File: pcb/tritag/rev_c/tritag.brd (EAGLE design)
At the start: 46.2 x 40 mm, 47 parts, among them J1 TC2030-JLINK-NL, J2 TC2030-JLINK-NL, J3 MICRO_USB_B_HIROSE_ZX62-B-5PA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, J4 BAT_HOLE, J5 BAT_HOLE, U1 NRF51822QF, U2 TRIPOINT, U3 LTC4065, U4 MAX8887EZK33+T, X1 EPSON-FA-128

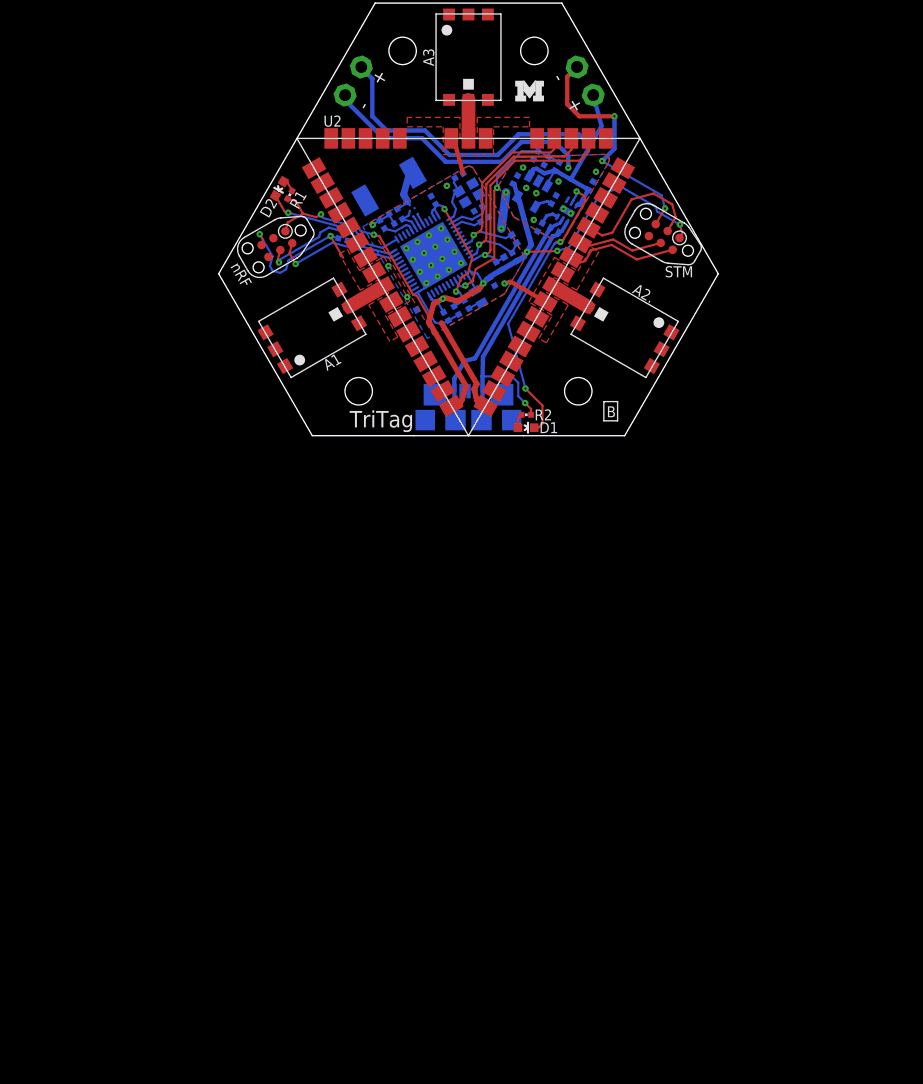
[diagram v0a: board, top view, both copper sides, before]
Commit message: added fundamental parts for TriTag
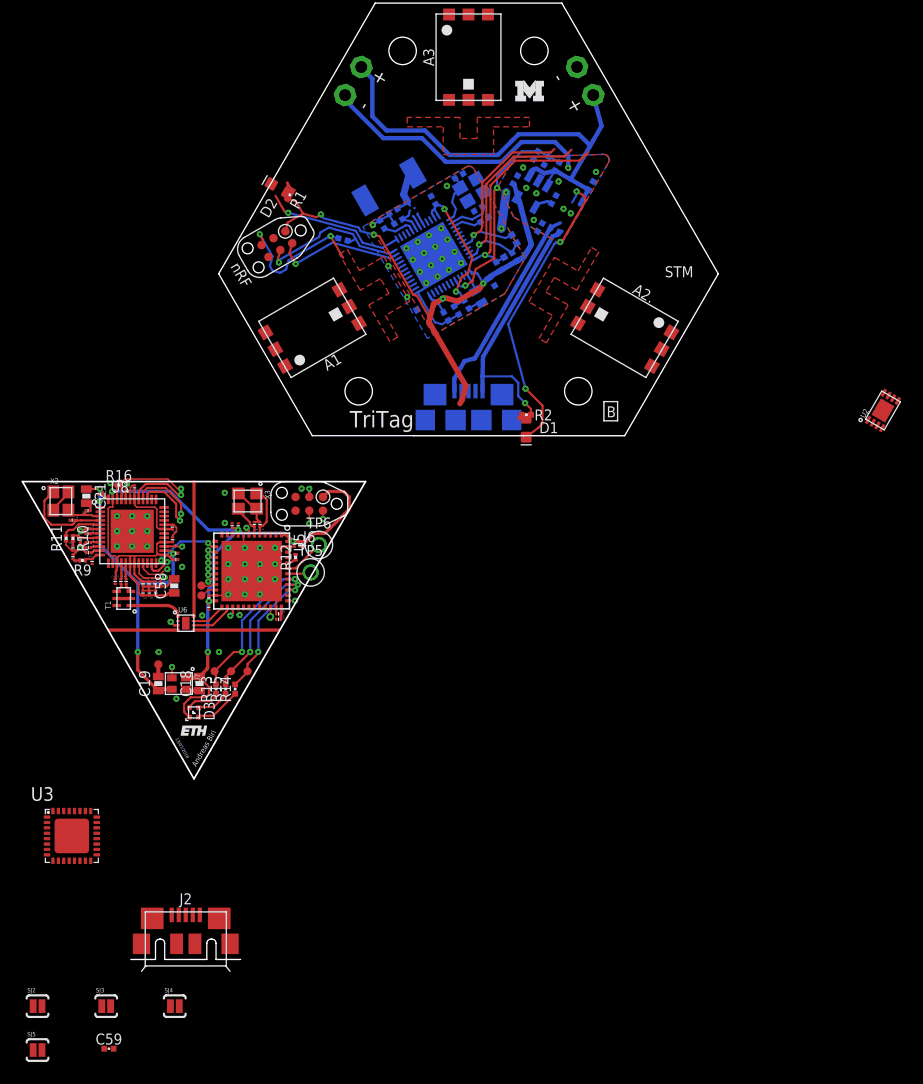
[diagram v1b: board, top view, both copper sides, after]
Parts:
- added C16, C17, C45, C46, C47, C48: 12pF, passives:0201_CAP
- added C18, C21, C58: 4.7uF, passives:0603_CAP
- added C19: 10uF, passives:0603_CAP
- added C20, C22, C23, C24, C25, C26, C27, C28, C29, C30, C36, C37, C38, C39, C40, C57: 0.1uF, passives:0201_CAP
- added C31, C32: 10pF, passives:0201_CAP
- added C33, C34: 330pF, passives:0201_CAP
- added C35: 0.01uF, passives:0201_CAP
- added C41: 820pF, passives:0201_CAP
- added C42: 27pF, passives:0201_CAP
- added C43: 1.2pF, passives:0201_CAP
- added C44: 18pF, passives:0201_CAP
- added C49, C50, C51, C53: 100nF, passives:0201_CAP
- added C52, C54: 4.7uF, passives:0201_CAP
- added C55: 10nF, passives:0201_CAP
- added C56: 1uF, passives:0201_CAP
- added C59: 0.1uF, passives:0402_CAP
- added D3: SML-LX0404SIUPGUSB, leds:1MM_SQ_4PAD
- added J6: TC2030-JLINK-NL, connector:TC2030-IDC-NL
- added R10: 16k, passives:0201_RES
- added R11, R12: 11k, passives:0201_RES
- added R13, R14, R15: 1k, passives:0402_RES
- added R16: 100k, passives:0201_RES
- added R9: 270, passives:0201_RES
- added SJ2, SJ3, SJ4, SJ5: SOLDERJUMPERNC2, SparkFun-Passives:SJ_2S-NOTRACE
- added T1: HHM1595A1, rf:EIA-0805
- added TP10, TP11, TP12, TP7, TP8, TP9: TEST-POINT, headers:PAD.03X.03
- added TP5, TP6: TEST_POINT_0.040IN, headers:TESTPOINT_0.040IN
- added U$1: (no value), logos:ETH_100MIL
- added U5: STM32F091CC, chips:UFQFPN-48
- added U6: SKY13317, switches:MLPQ-UT-8
- added U7: LXDC2HN18A, regulators:LXDC2HN
- added U8: DW1000, chips:QFN-48-DW1000
- added X2: 38.4M, crystals:FA-20H
- added X3: 16M, crystals:FA-20H
- J2: value TC2030-JLINK-NL -> MICRO_USB_B_HIROSE_ZX62R-B-5P(30); device connector:TC2030-IDC-NL -> connector:MICRO_USB_B_HIROSE_ZX62R-B-5P(30)
- R3: value 560 1% -> 2k 1%
- U2: value TRIPOINT -> MCP73831; device tripoint:TRIPOINT -> chips:DFN-8-MCP
- U3: value LTC4065 -> FT232RQ; device chips:DFN-6/2MM -> ftdichip:QFN32
- X1: value EPSON-FA-128 -> FA-20H; device crystals:FA-128 -> crystals:FA-20H
- moved J2 80.2 mm to (-26.2, -66.8), turned to 0 degrees
- moved U3 73.8 mm to (-36.7, -55.4), flipped to the top, turned to 0 degrees
- moved U2 41.6 mm to (38.4, -16.0), turned to 60 degrees
- moved X1 0.39 mm to (0.32, 4.40), turned to 240 degrees
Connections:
- removed net DW_INT: TP3.TP, U1.44, U2.38
- removed net I2C_SCL: R5.1, TP1.TP, U1.47, U2.37
- removed net I2C_SDA: R4.1, TP2.TP, U1.48, U2.36
- removed net N$2: A2..A, U2.26
- removed net N$3: A3.A, U2.43
- removed net N$4: J2.2, U2.28
- removed net N$7: J2.4, U2.29
- removed net N$8: J2.3, U2.30
- new net !DW_RST: U5.18, U8.27
- new net !DW_SPI_CS: U5.14, U8.24
- new net !FTDI_RESET: SJ3.2, U3.18
- new net !RST: SJ3.1
- new net !STM_RST: J6.3, U5.7
- new net +1V8: C19.1, C20.P$1, C21.1, C24.P$1, U7.3, U8.26, U8.48
- new net +3V3: C18.2, C31.P$1, C32.P$1, C33.P$1, C34.P$1, C35.P$1, C36.P$1, C37.P$1, C38.P$1, C39.P$1, C40.P$1, C49.P$1, C50.P$1, C51.P$1, C52.P$1, C53.P$1, C54.P$1, C55.P$1, C56.P$1, C58.1, D3.1, J6.1, U5.1, U5.24, U5.36, U5.48, U5.9, U7.1, U8.15, U8.18, U8.19, U8.25, U8.28, U8.47
- new net ANT_SEL1: U5.27, U6.3
- new net ANT_SEL2: U5.26, U6.6
- new net ANT_SEL3: U5.25, U6.7
- new net D+: J2.3, U3.14
- new net D-: J2.2, U3.15
- new net DBG_RX: SJ5.2
- new net DBG_TX: SJ4.2
- new net DW_IRQ: R16.2, U5.20, U8.45
- new net DW_SPI_CLK: U5.15, U8.41
- new net DW_SPI_MISO: U5.16, U8.40
- new net DW_SPI_MOSI: U5.17, U8.39
- new net DW_SYNC: U8.29
- new net DW_WAKEUP: U5.19, U8.23
- new net EXT_I2C_SCL: R5.1, TP1.TP, U1.47, U5.30
- new net EXT_I2C_SDA: R4.1, TP2.TP, U1.48, U5.31
- new net FTDI_VCCIO: SJ2.2, U3.1
- new net GPIO0: TP5.TESTPOINT, U5.42
- new net GPIO1: TP6.TESTPOINT, U5.43
- new net GPIO2: TP7.P$1, U5.21
- new net GPIO3: TP8.P$1, U5.22
- new net INTERRUPT: TP3.TP, U1.44, U5.12
- new net LED_BLUE: R15.2, TP10.P$1, U5.40
- new net LED_GREEN: R14.2, TP9.P$1, U5.39
- new net LED_RED: R13.2, TP11.P$1, U5.41
- new net N$12: T1.1, U6.1
- new net N$14: C16.P$2, T1.3
- new net N$16: C17.P$2, T1.4
- new net N$21: C41.P$1, R9.2
- new net N$22: C42.P$1, R10.2
- new net N$23: C44.P$1, R9.1, U8.12
- new net N$24: C43.P$1, R10.1, U8.8
- new net N$25: R11.2, U8.5
- new net N$26: R12.1, U5.44
- new net N$27: D3.4, R14.1
- new net N$28: D3.3, R15.1
- new net N$29: D3.2, R13.1
- new net OSC_IN: C47.P$1, U5.5, X3.1
- new net OSC_OUT: C48.P$1, U5.6, X3.3
- new net REG_EN: U7.2, U8.21
- new net RF1: A1.A, U6.4
- new net RF2: A2..A, U6.5
- new net RF3: A3.A, U6.8
- new net RF_N: C16.P$1, U8.17
- new net RF_P: C17.P$1, U8.16
- new net RXD: SJ4.1, U3.2
- new net STM_SWCLK: J6.4, U5.37
- new net STM_SWDIO: J6.2, U5.34
- new net TXD: SJ5.1, U3.30
- new net USB_5V: J2.1, U3.19
- new net VDDCLK: C26.P$1, U8.9
- new net VDDDIG: C22.P$1, C23.P$1, U8.20, U8.44
- new net VDDIF: C29.P$1, U8.7
- new net VDDIO: C28.P$1, C57.P$1, U8.31, U8.42
- new net VDDMS: C25.P$1, U8.6
- new net VDDSYN: C27.P$1, U8.10
- new net VDDVCO: C30.P$1, U8.11
- new net XTAL1: C46.P$1, U8.3, X2.3
- new net XTAL2: C45.P$1, U8.4, X2.1
- net GND: now also C18.1, C19.2, C20.P$2, C21.2, C22.P$2, C23.P$2, C24.P$2, C25.P$2, C26.P$2, C27.P$2, C28.P$2, C29.P$2, C30.P$2, C31.P$2, C32.P$2, C33.P$2, C34.P$2, C35.P$2, C36.P$2, C37.P$2, C38.P$2, C39.P$2, C40.P$2, C41.P$2, C42.P$2, C43.P$2, C44.P$2, C45.P$2, C46.P$2, C47.P$2, C48.P$2, C49.P$2, C50.P$2, C51.P$2, C52.P$2, C53.P$2, C54.P$2, C55.P$2, C56.P$2, C57.P$2, C58.2, C59.2, J6.5, R11.1, R12.2, R16.1, T1.2, T1.5, TP12.P$1, U2.6, U2.GND, U3.17, U3.20, U3.24, U3.26, U3.4, U5.23, U5.35, U5.47, U5.8, U5.GND, U6.GND, U7.4, U8.22, U8.32, U8.43, U8.46, U8.GND, X2.2, X2.4, X3.2, X3.4; no longer U2.10, U2.18, U2.25, U2.27, U2.42, U2.44, U2.8, U3.1, U3.5, U3.7
- net N$1: now also C59.1, U3.16; no longer A1.A, U2.9
- net N$13: now also U2.8; no longer U3.6
- net N$5: now also U2.5; no longer U3.2
- net VBAT: now also U2.3, U2.4; no longer U3.3
- net VCC: now also SJ2.1; no longer J2.1, U2.17
- net VUSB: now also U2.1, U2.2; no longer U3.4
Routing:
- net +3V3: track 0.00 -> 87.1 mm, vias 0 -> 5
- net +1V8: track 0.00 -> 31.5 mm, vias 0 -> 3
- net I2C_SCL: track 22.0 -> 0.00 mm, vias 1 -> 0
- net I2C_SDA: track 21.7 -> 0.00 mm, vias 1 -> 0
- net EXT_I2C_SCL: track 0.00 -> 21.0 mm, vias 0 -> 1
- net VCC: track 74.5 -> 54.0 mm, vias 7 -> 4
- net EXT_I2C_SDA: track 0.00 -> 20.5 mm, vias 0 -> 1
- net DW_IRQ: track 0.00 -> 20.4 mm, vias 0 -> 2
- net DW_INT: track 19.3 -> 0.00 mm, vias 1 -> 0
- net INTERRUPT: track 0.00 -> 18.3 mm, vias 0 -> 1
- net VDDDIG: track 0.00 -> 15.5 mm, vias 0 -> 2
- net LED_RED: track 0.00 -> 14.8 mm, vias 0 -> 2
- net DW_SPI_CLK: track 0.00 -> 14.5 mm, vias 0 -> 2
- net STM_SWDIO: track 0.00 -> 14.0 mm, vias 0 -> 2
- net REG_EN: track 0.00 -> 13.8 mm, vias 0 -> 2
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- added copper zone on layer 2, net GND
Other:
- board size 46.2 x 40 mm -> 64.4 x 71.8 mm
- board text added: "13/07/2018"
- board text added: "Andreas Biri"

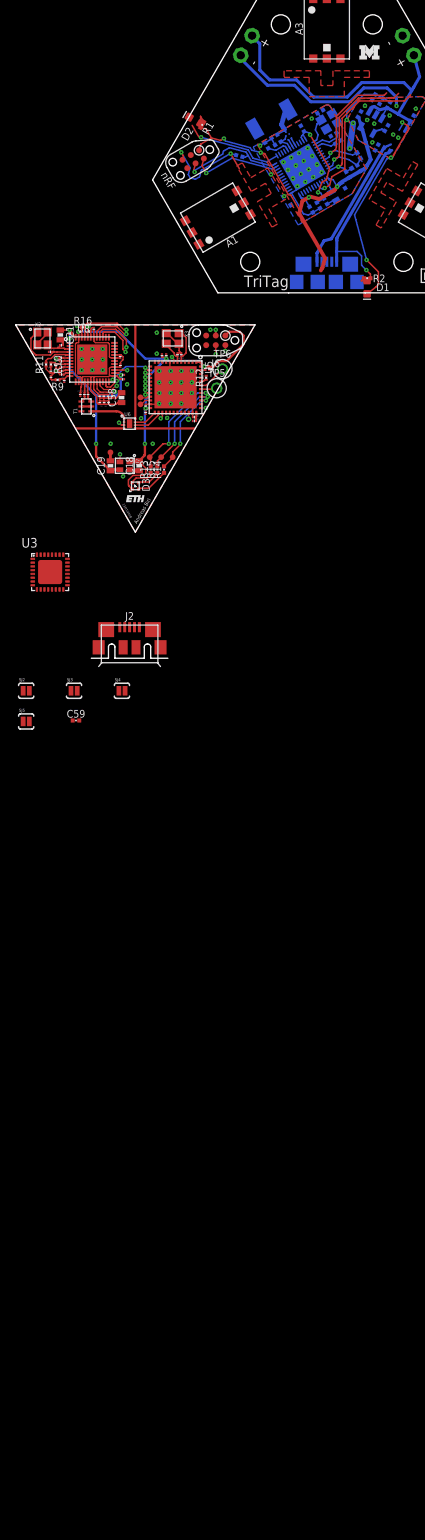
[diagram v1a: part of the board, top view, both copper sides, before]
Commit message: added all relevant parts for carrier board and started schematic
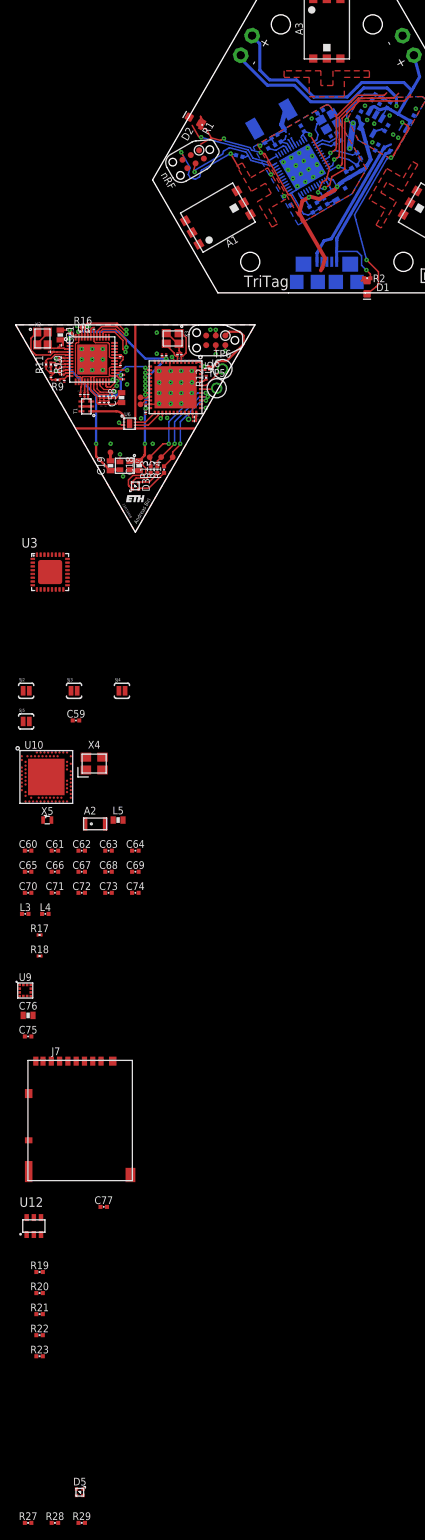
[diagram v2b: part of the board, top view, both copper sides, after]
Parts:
- removed J2: MICRO_USB_B_HIROSE_ZX62R-B-5P(30), connector:MICRO_USB_B_HIROSE_ZX62R-B-5P(30)
- removed LOGO1: UMICH_SOLID_SMALL, logos:UMICH_SOLID_75MIL
- added A2: ANT3216A063R2400A, chips:ANT3216A063R2400A
- added C60, C77: 4.7uF, passives:0402_CAP
- added C61, C62, C63, C64, C75: 0.1uF, passives:0402_CAP
- added C65, C71: 1uF, passives:0402_CAP
- added C66: 100pF, passives:0402_CAP
- added C67, C68, C73, C74: 12pF, passives:0402_CAP
- added C69: 0.8pF, passives:0402_CAP
- added C70: 0.5pF, passives:0402_CAP
- added C72: 47nF, passives:0402_CAP
- added C76: 10uF, passives:0603_CAP
- added D5: SML-LX0404SIUPGUSB, leds:1MM_SQ_4PAD
- added J7: CON_MICRO_SDDM3AT-SF-PEJM5, connector:DM3AT-SF-PEJM5
- added L3: 3.3nH, passives:0402_CAP
- added L4: 15nH, passives:0402_CAP
- added L5: 10uH, passives:0603_CAP
- added R17, R18: DNP, passives:0201_RES
- added R19, R20: 100k, passives:0402_RES
- added R21, R22, R23: 10k, passives:0402_RES
- added R27, R28, R29: 470, passives:0402_RES
- added U10: NRF52840, chips:AQFN73
- added U12: SIP32510, chips:TSOT23-6
- added U9: LIS2DW12, chips:LGA-12
- added X4: 32MHz, crystals:TXC-7V
- added X5: 32.768kHz, crystals:ABS05
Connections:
- removed net SWDIO/!RESET: J1.2, U1.23
- removed net USB_5V: J2.1, U3.19
- new net !NRF_CS_IMU: U10.AC17, U9.2
- new net !NRF_CS_SD: J7.2, R22.1, U10.AC15
- new net !RTC_IRQ1: U10.A16
- new net !RTC_IRQ2: U10.B15
- new net !RTC_IRQ3: U10.A14
- new net !SD_DETECT: J7.A, R20.1, U10.AD20
- new net LED_NRF_BLUE: R29.2, U10.K2
- new net LED_NRF_GREEN: R28.2, U10.L1
- new net LED_NRF_RED: R27.2, U10.J1
- new net N$2: C63.1, U10.C1
- new net N$3: C71.1, C72.1, L4.1, U10.B5, U10.E24
- new net N$4: C66.1, U10.D23
- new net N$51: C67.2, U10.B24, X4.3
- new net N$52: C68.2, U10.A23, X4.1
- new net N$53: L5.2, U10.B3
- new net N$54: L4.2, L5.1
- new net N$55: C77.1, J7.4, R20.2, R21.2, R22.2, R23.2, U12.1, U12.2
- new net N$59: D5.2, R27.1
- new net N$60: D5.4, R28.1
- new net N$61: D5.3, R29.1
- new net N$7: C69.1, L3.2, U10.H23
- new net N$8: A2.S1, C70.1, L3.1
- new net NRF_IMU_INT1: U10.AD16, U9.12
- new net NRF_IMU_INT2: U10.AD18, U9.11
- new net NRF_MISO: J7.7, R23.1, U10.R1, U9.3
- new net NRF_MOSI: J7.3, R21.1, U10.N1, U9.4
- new net NRF_SCK: J7.5, U9.1
- new net NRF_SWDCLK: J1.4, U10.AA24
- new net NRF_SWDIO: J1.2, U10.AC24
- new net RTC_CS: U10.B17
- new net SCK: U10.U1
- new net SD_EN: R19.1, U10.AC19, U12.3
- new net STM_INTERRUPT: TP3.TP, U1.44
- new net VBAT_OK: U10.R24
- new net VSEC: U10.A8
- new net VSOL: U10.B9
- new net WDI: U10.A12
- new net XL1: C74.2, U10.D2, X5.A
- new net XL2: C73.2, U10.F2, X5.B
- net !RST: now also U10.AC13
- net D+: now also J3.3; no longer J2.3
- net D-: now also J3.2; no longer J2.2
- net DBG_RX: now also U10.G1
- net DBG_TX: now also U10.H2
- net EXT_I2C_SCL: now also R17.1, U10.A20, U10.AC9
- net EXT_I2C_SDA: now also R18.1, U10.AD10, U10.B19
- net GND: now also A2.S2, C60.2, C61.2, C62.2, C63.2, C64.2, C65.2, C66.2, C67.1, C68.1, C69.2, C70.2, C71.2, C72.2, C73.1, C74.1, C75.2, C76.2, C77.2, J7.6, J7.B, J7.MOUNT0, J7.MOUNT1, J7.MOUNT2, J7.MOUNT3, R19.2, U10.AD2, U10.B7, U10.F23, U10.GND, U12.4, U9.5, U9.6, U9.7, U9.8, X4.2, X4.4; no longer J2.5
- net INTERRUPT: no longer TP3.TP, U1.44
- net SWDCLK: no longer J1.4
- net VBAT: now also U10.A10
- net VCC: now also C60.1, C61.1, C62.1, C64.1, C65.1, C75.1, C76.1, D5.1, R17.2, R18.2, U10.A22, U10.AD14, U10.AD23, U10.B1, U10.W1, U10.Y2, U12.5, U12.6, U9.10, U9.9
- net VUSB: now also U3.19
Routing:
- net STM_INTERRUPT: track 0.00 -> 18.3 mm, vias 0 -> 1
- net INTERRUPT: track 18.3 -> 0.00 mm, vias 1 -> 0
- net SWDIO/!RESET: track 12.2 -> 0.00 mm, vias 1 -> 0
- net VCC: track 54.0 -> 53.1 mm
- net GND: track 121.3 -> 120.8 mm
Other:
- board text added: "2018/07/14"
- board text removed: "2015/08/15"
- board text removed: "Brad Campbell"

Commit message: finished TriTag schematic
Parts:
- removed A1, A2., A3: TAIYO-YUDEN-AH086M, chips:TAIYO-YUDEN-AH086M
- removed B1: BAL-NRF01D3, chips:BAL-NRF01D3
- removed C61, C62, C63, C64: 0.1uF, passives:0402_CAP
- removed C65, C71: 1uF, passives:0402_CAP
- removed C66: 100pF, passives:0402_CAP
- removed C67, C68, C73, C74: 12pF, passives:0402_CAP
- removed C69: 0.8pF, passives:0402_CAP
- removed C70: 0.5pF, passives:0402_CAP
- removed C72: 47nF, passives:0402_CAP
- removed D2: BLUE, SparkFun-LED:LED-0603
- removed L3: 3.3nH, passives:0402_CAP
- removed L4: 15nH, passives:0402_CAP
- removed L5: 10uH, passives:0603_CAP
- removed R1: 1k, passives:0402_RES
- removed R17, R18: DNP, passives:0201_RES
- removed R6: 12k, passives:0402_RES
- removed U10: NRF52840, chips:AQFN73
- removed X5: 32.768kHz, crystals:ABS05
- added A2.1, A5: TAIYO-YUDEN-AH086M, chips:TAIYO-YUDEN-AH086M
- added C78: 1pF, passives:0402_CAP
- added C79: 1uF, passives:0402_CAP
- added C80: 47nF, passives:0402_CAP
- added C81, C82: 12pF, passives:0402_CAP
- added L6: 10uH, passives:0603_CAP
- A2: value ANT3216A063R2400A -> TAIYO-YUDEN-AH086M; device chips:ANT3216A063R2400A -> chips:TAIYO-YUDEN-AH086M
- A4: value FRACTUS-2.4GHZ-FR05-S1-N-0-102 -> ANT3216A063R2400A; device chips:FRACTUS-ANTENNA-FR05-S1-N-0-102 -> chips:ANT3216A063R2400A
- C1: value 0.8pF -> 4.7uF
- C12: value 1uF -> 12pF
- C14: value 4.7uF -> 1pF
- C2, C3: value 12pF -> 0.1uF
- C4: value 1nF -> 0.1uF
- C5: value 2.2nF -> 0.1uF
- C6: value 47nF -> 1uF
- C60: value 4.7uF -> 820pF
- C7: value 0.1uF -> 100pF
- C8: value 0.1uF -> 12pF
- L1: value 15nH -> 3.9nH
- L2: value 10uH -> 15nH; device passives:0603_CAP -> passives:0402_CAP
- R4, R5: value 10k -> DNP
- U1: value NRF51822QF -> NRF52840; device chips:QFN-48-6MM -> chips:AQFN73
- X1: value FA-20H -> 32MHz; device crystals:FA-20H -> crystals:TXC-7V
- X4: value 32MHz -> 32.768kHz; device crystals:TXC-7V -> crystals:ABS05
- moved C3 213.6 mm to (-37.3, -204.7), flipped to the top, turned to 0 degrees
- moved C2 211.4 mm to (-40.0, -204.7), flipped to the top, turned to 0 degrees
- moved C4 210.5 mm to (-34.7, -204.7), flipped to the top, turned to 0 degrees
- moved C7 208.3 mm to (-26.7, -204.7), flipped to the top, turned to 0 degrees
- moved C5 207.8 mm to (-32.0, -204.7), flipped to the top, turned to 0 degrees
- moved C6 207.0 mm to (-29.3, -204.7), flipped to the top, turned to 0 degrees
- moved A4 206.3 mm to (-39.2, -199.1), flipped to the top, turned to 0 degrees
- moved C1 205.2 mm to (-25.9, -201.9), flipped to the top, turned to 0 degrees
- moved L2 205.1 mm to (-34.7, -207.5), flipped to the top, turned to 0 degrees
- moved L1 204.7 mm to (-37.3, -207.5), flipped to the top, turned to 0 degrees
- moved C8 203.8 mm to (-40.0, -207.5), flipped to the top, turned to 0 degrees
- moved C14 196.9 mm to (-29.6, -198.4), flipped to the top, turned to 0 degrees
- moved C12 194.3 mm to (-33.1, -198.4), flipped to the top, turned to 0 degrees
- moved X1 193.7 mm to (-30.9, -186.8), flipped to the top, turned to 0 degrees
- moved U1 190.0 mm to (-37.2, -188.6), flipped to the top, turned to 0 degrees
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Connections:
- removed net !CHRG1: D2.A, R1.1
- removed net !RTC_IRQ1: U10.A16
- removed net !RTC_IRQ2: U10.B15
- removed net !RTC_IRQ3: U10.A14
- removed net ANTENNA: A4.1, B1.SE, C1.1
- removed net AVDD: C12.1, C4.1, L1.1, U1.35, U1.36
- removed net DCC: L2.2, U1.2
- removed net N$3: C71.1, C72.1, L4.1, U10.B5, U10.E24
- removed net N$4: C66.1, U10.D23
- removed net N$51: C67.2, U10.B24, X4.3
- removed net N$52: C68.2, U10.A23, X4.1
- removed net N$53: L5.2, U10.B3
- removed net N$54: L4.2, L5.1
- removed net N$7: C69.1, L3.2, U10.H23
- removed net N$8: A2.S1, C70.1, L3.1
- removed net RTC_CS: U10.B17
- removed net SWDCLK: R6.2, U1.24
- removed net WDI: U10.A12
- removed net XL1: C74.2, U10.D2, X5.A
- removed net XL2: C73.2, U10.F2, X5.B
- new net XL3: C82.2, U1.D2, X4.A
- new net XL4: C81.2, U1.F2, X4.B
- net !NRF_CS_IMU: now also U1.AC17; no longer U10.AC17
- net !NRF_CS_SD: now also U1.AC15; no longer U10.AC15
- net !RST: now also U1.AC13; no longer U10.AC13
- net !SD_DETECT: now also U1.AD20; no longer U10.AD20
- net BATIN: now also U1.P23; no longer U1.5
- net DBG_RX: now also U1.G1; no longer U10.G1
- net DBG_TX: now also U1.H2; no longer U10.H2
- net EXT_I2C_SCL: now also U1.A20, U1.AC9; no longer R17.1, U1.47, U10.A20, U10.AC9
- net EXT_I2C_SDA: now also U1.AD10, U1.B19; no longer R18.1, U1.48, U10.AD10, U10.B19
- net GND: now also A4.S2, C12.1, C78.2, C79.2, C8.1, C80.2, C81.1, C82.1, U1.AD2, U1.B7, U1.F23; no longer A2.S2, B1.GND, C12.2, C61.2, C62.2, C63.2, C64.2, C65.2, C66.2, C67.1, C68.1, C69.2, C70.2, C71.2, C72.2, C73.1, C74.1, C8.2, R6.1, U1.13, U1.33, U1.34, U10.AD2, U10.B7, U10.F23, U10.GND, X4.2, X4.4
- net LED_NRF_BLUE: now also U1.K2; no longer U10.K2
- net LED_NRF_GREEN: now also U1.L1; no longer U10.L1
- net LED_NRF_RED: now also U1.J1; no longer U10.J1
- net N$10: now also C7.1, U1.D23; no longer C2.1, U1.38, X1.3
- net N$15: now also C14.1, L1.2, U1.H23; no longer C6.1, U1.29
- net N$17: now also A4.S1, C78.1, L1.1; no longer C7.1, U1.39
- net N$18: now also C8.2, U1.B24, X1.3; no longer B1.ANT1, U1.31
- net N$19: now also C12.2, U1.A23, X1.1; no longer B1.ANT2, U1.32
- net N$2: now also C60.1, U1.N24; no longer C63.1, U10.C1
- net N$20: now also L6.2, U1.B3; no longer B1.VCC, C5.1, U1.30
- net N$37: now also L2.2, L6.1; no longer L1.2, L2.1
- net N$6: now also C4.1, U1.C1; no longer D2.C, U1.25
- net N$9: now also C79.1, C80.1, L2.1, U1.B5, U1.E24; no longer C3.1, U1.37, X1.1
- net NRF_IMU_INT1: now also U1.AD16; no longer U10.AD16
- net NRF_IMU_INT2: now also U1.AD18; no longer U10.AD18
- net NRF_MISO: now also U1.R1; no longer U10.R1
- net NRF_MOSI: now also U1.N1; no longer U10.N1
- net NRF_SWDCLK: now also U1.AA24; no longer U10.AA24
- net NRF_SWDIO: now also U1.AC24; no longer U10.AC24
- net RF1: now also A5.A; no longer A1.A
- net RF2: now also A2.1.A; no longer A2..A
- net RF3: now also A2.A; no longer A3.A
- net SCK: now also U1.U1; no longer U10.U1
- net SD_EN: now also U1.AC19; no longer U10.AC19
- net STM_INTERRUPT: now also U1.B17; no longer U1.44
- net VBAT: now also U1.A10; no longer U10.A10
- net VBAT_OK: now also U1.R24; no longer U10.R24
- net VCC: now also C1.1, C2.1, C3.1, C5.1, C6.1, U1.A22, U1.AD14, U1.AD23, U1.B1, U1.W1, U1.Y2; no longer C14.1, C60.1, C61.1, C62.1, C64.1, C65.1, C8.1, R1.2, R17.2, R18.2, U1.1, U1.12, U10.A22, U10.AD14, U10.AD23, U10.B1, U10.W1, U10.Y2
- net VSEC: now also U1.A8; no longer U10.A8
- net VSOL: now also U1.B9; no longer U10.B9
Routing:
- net GND: track 120.8 -> 96.6 mm, vias 50 -> 46
- net BATIN: track 19.9 -> 0.00 mm, vias 2 -> 0
- net SWDCLK: track 14.7 -> 0.00 mm, vias 1 -> 0
- net AVDD: track 14.2 -> 0.00 mm, vias 2 -> 0
- net N$6: track 13.3 -> 0.00 mm, vias 1 -> 0
- net N$10: track 5.24 -> 0.00 mm
- net ANTENNA: track 4.71 -> 0.00 mm
- net N$9: track 4.53 -> 0.00 mm
- net N$15: track 3.00 -> 0.00 mm
- net N$20: track 2.75 -> 0.00 mm
- net N$17: track 2.67 -> 0.00 mm
- net VCC: track 53.1 -> 50.8 mm
- net !CHRG1: track 1.86 -> 0.00 mm
- net DCC: track 1.78 -> 0.00 mm
- net N$37: track 1.36 -> 0.00 mm
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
